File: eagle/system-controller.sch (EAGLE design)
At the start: 221 parts, among them IC1 TS4100, Q1 MOSFET-P-N-PAIR, Q10 MOSFET-P-N-PAIR, Q11 MOSFET-P-N-PAIR, Q12 MOSFET-P-N-PAIR, Q13 MOSFET-P-N-PAIR, Q14 MOSFET-P-N-PAIR, Q15 MOSFET-P-N-PAIR, Q16 MOSFET-P-N-PAIR, Q17 MOSFET-P-N-PAIR, Q18 MOSFET-P-N-PAIR, Q19 MOSFET-P-N-PAIR, Q2 MOSFET-P-N-PAIR, Q3 DNP/NTR4101P, Q4 DNP/NTR4101P, Q5 DNP/NTR4101P, Q6 DNP/NTR4101P, Q7 MOSFET-P-N-PAIR, Q8 MOSFET-P-N-PAIR, Q9 MOSFET-P-N-PAIR, SW1 TPS25944LRVCRWQFN-20-3X4, SW2 TPS25944LRVCRWQFN-20-3X4, SW3 TPS25944LRVCRWQFN-20-3X4, SW4 TPS25944LRVCRWQFN-20-3X4, SW5 TPS25944LRVCRWQFN-20-3X4, SW6 TPS25944LRVCRWQFN-20-3X4, SW7 TPS25944LRVCRWQFN-20-3X4, SW8 TPS25944LRVCRWQFN-20-3X4, U1 MEGA128-A, X1 8 MHz CRYSTAL-ABRACON-ABM3-SMD

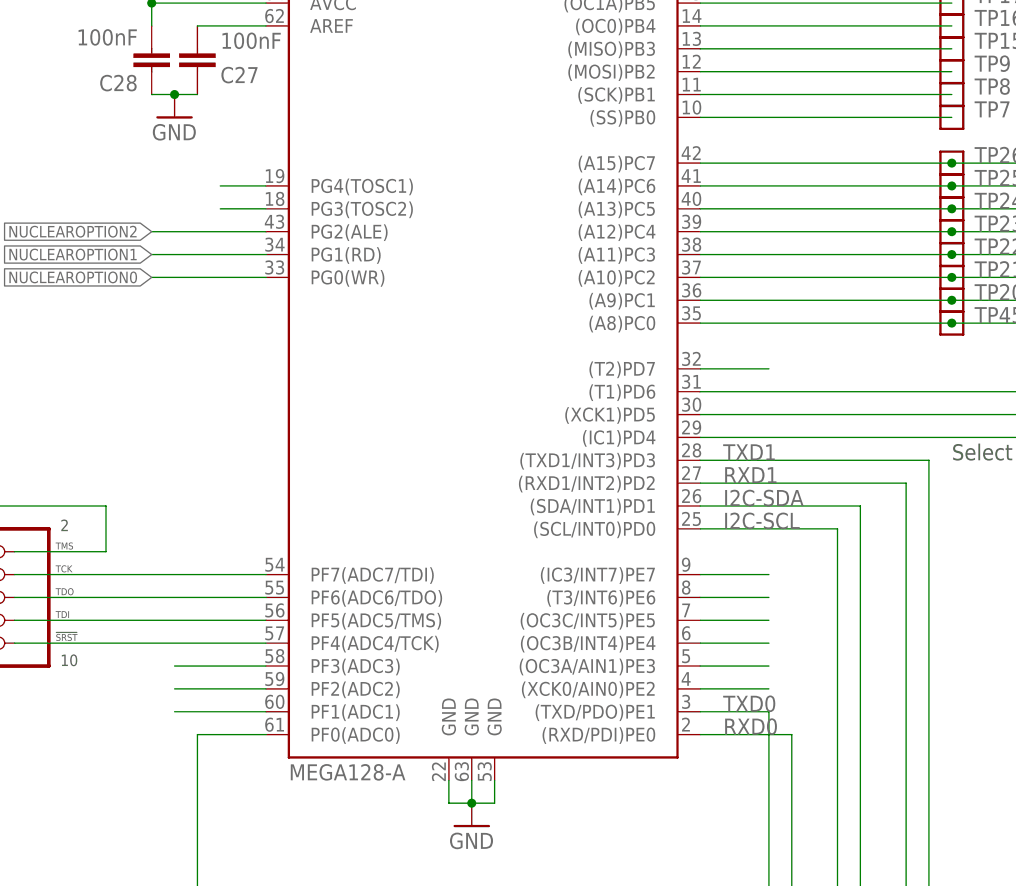
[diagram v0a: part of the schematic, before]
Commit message: added the remaining test points
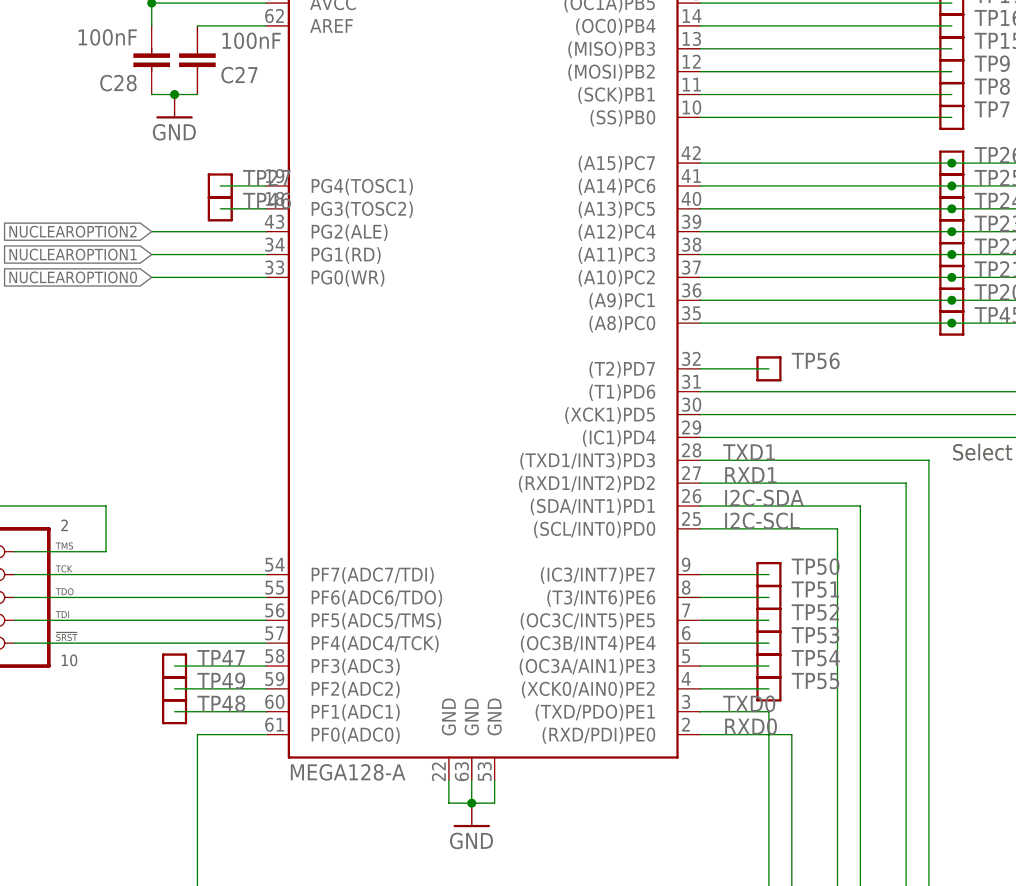
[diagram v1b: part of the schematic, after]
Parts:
- added TP27, TP46, TP47, TP48, TP49, TP50, TP51, TP52, TP53, TP54, TP55, TP56: TEST-POINT, Tova:TEST-POINT
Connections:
- net N$104: now also TP56.1
- net N$27: now also TP46.1
- net N$28: now also TP27.1
- net N$34: now also TP47.1
- net N$35: now also TP49.1
- net N$37: now also TP48.1
- net N$39: now also TP55.1
- net N$40: now also TP54.1
- net N$41: now also TP53.1
- net N$42: now also TP52.1
- net N$43: now also TP51.1
- net N$44: now also TP50.1
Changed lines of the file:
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@@
 <?xml version="1.0" encoding="utf-8"?>
 <!DOCTYPE eagle SYSTEM "eagle.dtd">
-<eagle version="7.3.0">
+<eagle version="7.5.0">
 <drawing>
 <settings>
@@
 <setting verticaltext="up"/>
 </settings>
-<grid distance="0.05" unitdist="inch" unit="inch" style="lines" multiple="2" display="yes" altdistance="0.01" altunitdist="inch" altunit="inch"/>
+<grid distance="0.1" unitdist="inch" unit="inch" style="lines" multiple="1" display="no" altdistance="0.01" altunitdist="inch" altunit="inch"/>
 <layers>
 <layer number="1" name="Top" color="4" fill="1" visible="no" active="no"/>
@@
 <attribute name="MPN" value="Vishay"/>
 </part>
+<part name="TP27" library="Tova" deviceset="TEST-POINT" device=""/>
+<part name="TP46" library="Tova" deviceset="TEST-POINT" device=""/>
+<part name="TP47" library="Tova" deviceset="TEST-POINT" device=""/>
+<part name="TP48" library="Tova" deviceset="TEST-POINT" device=""/>
+<part name="TP49" library="Tova" deviceset="TEST-POINT" device=""/>
+<part name="TP50" library="Tova" deviceset="TEST-POINT" device=""/>
+<part name="TP51" library="Tova" deviceset="TEST-POINT" device=""/>
+<part name="TP52" library="Tova" deviceset="TEST-POINT" device=""/>
+<part name="TP53" library="Tova" deviceset="TEST-POINT" device=""/>
+<part name="TP54" library="Tova" deviceset="TEST-POINT" device=""/>
+<part name="TP55" library="Tova" deviceset="TEST-POINT" device=""/>
+<part name="TP56" library="Tova" deviceset="TEST-POINT" device=""/>
 </parts>
 <sheets>
@@
 <attribute name="MPN" x="102.87" y="317.5" size="1.778" layer="96" rot="R180" display="off"/>
 </instance>
+<instance part="TP27" gate="G$1" x="149.86" y="220.98" smashed="yes">
+<attribute name="NAME" x="152.4" y="220.98" size="1.778" layer="95" font="vector"/>
+</instance>
+<instance part="TP46" gate="G$1" x="149.86" y="218.44" smashed="yes">
+<attribute name="NAME" x="152.4" y="218.44" size="1.778" layer="95" font="vector"/>
+</instance>
+<instance part="TP47" gate="G$1" x="144.78" y="167.64" smashed="yes">
+<attribute name="NAME" x="147.32" y="167.64" size="1.778" layer="95" font="vector"/>
+</instance>
+<instance part="TP48" gate="G$1" x="144.78" y="162.56" smashed="yes">
+<attribute name="NAME" x="147.32" y="162.56" size="1.778" layer="95" font="vector"/>
+</instance>
+<instance part="TP49" gate="G$1" x="144.78" y="165.1" smashed="yes">
+<attribute name="NAME" x="147.32" y="165.1" size="1.778" layer="95" font="vector"/>
+</instance>
+<instance part="TP50" gate="G$1" x="210.82" y="177.8" smashed="yes">
+<attribute name="NAME" x="213.36" y="177.8" size="1.778" layer="95" font="vector"/>
+</instance>
+<instance part="TP51" gate="G$1" x="210.82" y="175.26" smashed="yes">
+<attribute name="NAME" x="213.36" y="175.26" size="1.778" layer="95" font="vector"/>
+</instance>
+<instance part="TP52" gate="G$1" x="210.82" y="172.72" smashed="yes">
+<attribute name="NAME" x="213.36" y="172.72" size="1.778" layer="95" font="vector"/>
+</instance>
+<instance part="TP53" gate="G$1" x="210.82" y="170.18" smashed="yes">
+<attribute name="NAME" x="213.36" y="170.18" size="1.778" layer="95" font="vector"/>
+</instance>
+<instance part="TP54" gate="G$1" x="210.82" y="167.64" smashed="yes">
+<attribute name="NAME" x="213.36" y="167.64" size="1.778" layer="95" font="vector"/>
+</instance>
+<instance part="TP55" gate="G$1" x="210.82" y="165.1" smashed="yes">
+<attribute name="NAME" x="213.36" y="165.1" size="1.778" layer="95" font="vector"/>
+</instance>
+<instance part="TP56" gate="G$1" x="210.82" y="200.66" smashed="yes">
+<attribute name="NAME" x="213.36" y="200.66" size="1.778" layer="95" font="vector"/>
+</instance>
 </instances>
 <busses>
@@
 <pinref part="U1" gate="G$1" pin="PG3(TOSC2)"/>
 <wire x1="154.94" y1="218.44" x2="149.86" y2="218.44" width="0.1524" layer="91"/>
+<pinref part="TP46" gate="G$1" pin="1"/>
 </segment>
 </net>
@@
 <pinref part="U1" gate="G$1" pin="PG4(TOSC1)"/>
 <wire x1="154.94" y1="220.98" x2="149.86" y2="220.98" width="0.1524" layer="91"/>
+<pinref part="TP27" gate="G$1" pin="1"/>
 </segment>
 </net>
@@
 <pinref part="U1" gate="G$1" pin="PF3(ADC3)"/>
 <wire x1="154.94" y1="167.64" x2="144.78" y2="167.64" width="0.1524" layer="91"/>
+<pinref part="TP47" gate="G$1" pin="1"/>
 </segment>
 </net>
@@
 <pinref part="U1" gate="G$1" pin="PF2(ADC2)"/>
 <wire x1="144.78" y1="165.1" x2="154.94" y2="165.1" width="0.1524" layer="91"/>
+<pinref part="TP49" gate="G$1" pin="1"/>
 </segment>
 </net>
@@
 <pinref part="U1" gate="G$1" pin="PF1(ADC1)"/>
 <wire x1="154.94" y1="162.56" x2="144.78" y2="162.56" width="0.1524" layer="91"/>
+<pinref part="TP48" gate="G$1" pin="1"/>
 </segment>
 </net>
@@
 <pinref part="U1" gate="G$1" pin="(XCK0/AIN0)PE2"/>
 <wire x1="203.2" y1="165.1" x2="210.82" y2="165.1" width="0.1524" layer="91"/>
+<pinref part="TP55" gate="G$1" pin="1"/>
 </segment>
 </net>
@@
 <pinref part="U1" gate="G$1" pin="(OC3A/AIN1)PE3"/>
 <wire x1="203.2" y1="167.64" x2="210.82" y2="167.64" width="0.1524" layer="91"/>
+<pinref part="TP54" gate="G$1" pin="1"/>
 </segment>
 </net>
@@
 <pinref part="U1" gate="G$1" pin="(OC3B/INT4)PE4"/>
 <wire x1="203.2" y1="170.18" x2="210.82" y2="170.18" width="0.1524" layer="91"/>
+<pinref part="TP53" gate="G$1" pin="1"/>
 </segment>
 </net>
@@
 <pinref part="U1" gate="G$1" pin="(OC3C/INT5)PE5"/>
 <wire x1="203.2" y1="172.72" x2="210.82" y2="172.72" width="0.1524" layer="91"/>
+<pinref part="TP52" gate="G$1" pin="1"/>
 </segment>
 </net>
@@
 <pinref part="U1" gate="G$1" pin="(T3/INT6)PE6"/>
 <wire x1="203.2" y1="175.26" x2="210.82" y2="175.26" width="0.1524" layer="91"/>
+<pinref part="TP51" gate="G$1" pin="1"/>
 </segment>
 </net>
@@
 <pinref part="U1" gate="G$1" pin="(IC3/INT7)PE7"/>
 <wire x1="203.2" y1="177.8" x2="210.82" y2="177.8" width="0.1524" layer="91"/>
+<pinref part="TP50" gate="G$1" pin="1"/>
 </segment>
 </net>
@@
 <pinref part="U1" gate="G$1" pin="(T2)PD7"/>
 <wire x1="203.2" y1="200.66" x2="210.82" y2="200.66" width="0.1524" layer="91"/>
+<pinref part="TP56" gate="G$1" pin="1"/>
 </segment>
 </net>

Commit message: working on board layout. Have everything organized in in general location. Working on routing.
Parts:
- removed C10, C18, C20, C22, C24: TBD, rcl_custom:C-EU0603-B-NOSILK
- removed C19, C29: 1uF, rcl_custom:C-EU0603-B-NOSILK
- removed LED13, LED14, LED15: DNP/AMB, psas_c3_team05:LED-0603
- removed Q14, Q15, Q16, Q17, Q18, Q19, Q8: MOSFET-P-N-PAIR, ic-transistor-mosfet-n-p:MOSFET-P-N-PAIR
- removed Q20: (no value), adafruit:MOSFET-NREFLOW
- removed R47, R53: 4.7k, rcl_custom:R-US_0603-B-NOSILK
- removed R48, R49, R54, R55: 47k, rcl_custom:R-US_0603-B-NOSILK
- removed R51, R56: 1k, rcl_custom:R-US_0603-B-NOSILK
- removed RUVLO1, RUVLO2, RUVLO3, RUVLO4, RUVLO5, RUVLO6, RUVLO7, RUVLO8: 93.1k, rcl_custom:R-US_0603-B-NOSILK
- removed SW8: TPS25944LRVCRWQFN-20-3X4, WQFN-20-3x4:TPS25944LRVCRWQFN-20-3X4
- removed TP1: TPSPAD1-13, testpad:TPSPAD1-13
- added CFUSE3A: 1uF, rcl_custom:C-EU0603-B-NOSILK
- added CFUSE7: TBD, rcl_custom:C-EU0603-B-NOSILK
- added CLDO3: 2.2uF, rcl_custom:C-EU0603-B-NOSILK
- added CPHOTO0A, CPHOTO1B, CPHOTO3A, CPHOTO3B: 100nF, rcl_custom:C-EU0603-B-NOSILK
- added LED0, LED4, LED5: GRN, psas_c3_team05:LED-0603
- added Q0: MOSFET-P-N-PAIR, ic-transistor-mosfet-n-p:MOSFET-P-N-PAIR
- added R0/UVLO, R1/UVLO, R2/UVLO, R3/UVLO, R4/UVLO, R5/UVLO, R6/UVLO, R7/UVLO: 47k, rcl_custom:R-US_0603-B-NOSILK
- added RLDO1: 10k, rcl_custom:R-US_0603-B-NOSILK
- added RPHOTO0A, RPHOTO0B, RPHOTO1A, RPHOTO2A, RPHOTO2B, RPHOTO3A, RPHOTO3B: 390, rcl_custom:R-US_0603-B-NOSILK
- added SW0: TPS25944LRVCRWQFN-20-3X4, WQFN-20-3x4:TPS25944LRVCRWQFN-20-3X4
- added TPLDOA: TEST-POINT, Tova:TEST-POINT
- C11, C13, C15, C17, C9: value 1uF -> TBD; DIST digikey -> (none); DPN 1276-1946-1-ND -> (none); MFN Samsung -> (none); MPN CL10B105KP8NNNC -> (none)
- C12, C14, C16: value TBD -> 1uF; DIST (none) -> digikey; DPN (none) -> 1276-1946-1-ND; MFN (none) -> Samsung; MPN (none) -> CL10B105KP8NNNC
- C2: value 100nF -> 1uF; DPN 399-1097-1-ND -> 1276-1946-1-ND; MFN Kemet -> Samsung; MPN C0603C104J4RACTU -> CL10B105KP8NNNC
- C3: value 100nF -> TBD; DIST digikey -> (none); DPN 490-6327-1-ND -> (none); MFN Murata -> (none); MPN GRM155R71C104JA88D -> (none)
- C4: value 2.2uF -> 1uF; DPN 1276-1183-1-ND -> 1276-1946-1-ND; MPN CL10A225KQ8NNNC -> CL10B105KP8NNNC
- C5: value 100nF -> TBD; DIST digikey -> (none); DPN 399-1097-1-ND -> (none); MFN Kemet -> (none); MPN C0603C104J4RACTU -> (none)
- C6: value 100nF -> 1uF; DPN 490-6327-1-ND -> 1276-1946-1-ND; MFN Murata -> Samsung; MPN GRM155R71C104JA88D -> CL10B105KP8NNNC
- LED10, LED11, LED12, LED9: value GRN -> DNP/AMB; DPN 732-4971-1-ND -> 475-2712-1-ND; MFN Wurth Electronics INC. -> OSRAM Opto Semi,; MPN 150060GS75000 -> LA L296-Q2R2-1-Z
- LED6: value DNP/AMB -> GRN; DPN 475-2712-1-ND -> 732-4971-1-ND; MFN OSRAM Opto Semi, -> Wurth Electronics INC.; MPN LA L296-Q2R2-1-Z -> 150060GS75000
- Q10, Q11, Q12, Q9: value MOSFET-P-N-PAIR -> DNP/NTR4101P; device ic-transistor-mosfet-n-p:MOSFET-P-N-PAIR -> Tova:NTR4101P; DPN DMG6601LVT-7DICT-ND -> NTR4101PT1HOSCT-ND; MFN Diodes Incorporated -> ON Semiconductor; MPN DMG6601LVT-7 -> NTR4101PT1H
- Q13: value MOSFET-P-N-PAIR -> (none); device ic-transistor-mosfet-n-p:MOSFET-P-N-PAIR -> adafruit:MOSFET-NREFLOW; DIST digikey -> (none); DPN DMG6601LVT-7DICT-ND -> (none); MFN Diodes Incorporated -> (none); MPN DMG6601LVT-7 -> (none)
- Q3, Q4, Q5, Q6: value DNP/NTR4101P -> MOSFET-P-N-PAIR; device Tova:NTR4101P -> ic-transistor-mosfet-n-p:MOSFET-P-N-PAIR; DPN NTR4101PT1HOSCT-ND -> DMG6601LVT-7DICT-ND; MFN ON Semiconductor -> Diodes Incorporated; MPN NTR4101PT1H -> DMG6601LVT-7
- R1, R3, R7: value 390 -> 47k; DPN A103093CT-ND -> 1276-4808-1-ND; MFN TE -> Samaung; MPN 4-1676481-5 -> RC1608F473CS
- R10, R5: value 390 -> 93.1k; DPN A103093CT-ND -> 1276-4837-1-ND; MFN TE -> Samsung; MPN 4-1676481-5 -> RC1608F9312CS
- R12: value 10k -> 1k; DPN 1276-3485-1-ND -> 1276-3484-1-ND; MPN RC1608F103CS -> RC1608F102CS
- R14, R20, R28, R33, R38, R43: value 47k -> 4.7k; DPN 1276-4808-1-ND -> 1276-3502-1-ND; MFN Samaung -> Samsung; MPN RC1608F473CS -> RC1608F472CS
- R15, R21: value 1k -> 47k; DPN 1276-3484-1-ND -> 1276-4808-1-ND; MFN Samsung -> Samaung; MPN RC1608F102CS -> RC1608F473CS
- R16, R25: value 47k -> 93.1k; DPN 1276-4808-1-ND -> 1276-4837-1-ND; MFN Samaung -> Samsung; MPN RC1608F473CS -> RC1608F9312CS
- R18: value 4.7k -> 1k; DPN 1276-3502-1-ND -> 1276-3484-1-ND; MPN RC1608F472CS -> RC1608F102CS
- R2, R8: value 390 -> 4.7k; DPN A103093CT-ND -> 1276-3502-1-ND; MFN TE -> Samsung; MPN 4-1676481-5 -> RC1608F472CS
- R26, R31, R36, R41, R46, R6: value 47k -> 1k; DPN 1276-4808-1-ND -> 1276-3484-1-ND; MFN Samaung -> Samsung; MPN RC1608F473CS -> RC1608F102CS
- R27, R32, R37, R42, R9: value 4.7k -> 47k; DPN 1276-3502-1-ND -> 1276-4808-1-ND; MFN Samsung -> Samaung; MPN RC1608F472CS -> RC1608F473CS
- R30, R35, R40, R45: value 1k -> 93.1k; DPN 1276-3484-1-ND -> 1276-4837-1-ND; MPN RC1608F102CS -> RC1608F9312CS
- SW1: DIST digikey -> (none); DPN 296-42152-1-ND -> (none); MFN TPS25944LRVCR -> (none); MPN Texas Instruments -> (none)
- renumbered C21 to CFUSE7A, C23 to CLDO1, C31 to CHWWD, C40 to CLDO2, LED8 to LED3, R11 to RA4, R17 to RA2, R50 to RA1, R52 to RHWWD0, R57 to RA3, R58 to RA5, R59 to RA7, R60 to RA8, R62 to RA6, R63 to RPHOTO1B, R64 to RHWWD1, R65 to RHWWD2, R66 to RHWWD4, R67 to RHWWD3, RILIM to RILIM0, RIMON to RIMON0, TP28 to TP0GHT, TP29 to TP1GOOD, TP30 to TP1GHT, TP31 to TP2GOOD, TP32 to TP2GHT, TP33 to TP3GOOD, TP34 to TP3GHT, TP35 to TP4GOOD, TP36 to TP4GHT, TP37 to TP5GOOD, TP38 to TP5GHT, TP39 to TP6GOOD, TP40 to TP6GHT, TP41 to TP7GOOD, TP42 to TP7GHT, TP5 to TP0GOOD
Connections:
- removed net N$31: C10.1, SW1.DV/DT
- removed net N$7: Q2A.D, Q2B.G, R14.2
- new net C10\: CFUSE3A.2, Q3B.S, R19.1, SW3.IN
- new net INOF: C3.1, SW0.DV/DT
- new net N$110: Q7B.D, R45.1
- new net N$111: Q6B.D, R40.1
- net 3V: now also CLDO3.1, CPHOTO1B.2, CPHOTO3B.2, Q10.S, Q11.S, Q12.S, Q9.S, U$2.VDD; no longer C2.2, C4.1, C6.2, Q3.S, Q4.S, Q5.S, Q6.S, U$3.VDD
- net GND: now also C11.2, C12.1, C13.2, C14.1, C15.2, C16.1, C17.2, C3.2, C4.1, C5.2, C9.2, CFUSE3A.1, CFUSE7.2, CLDO3.2, CPHOTO0A.1, CPHOTO1B.1, CPHOTO3A.1, CPHOTO3B.1, LED0.K, LED4.K, LED5.K, Q0A.S, Q13.S, Q3A.S, Q4A.S, Q5A.S, Q6A.S, R0/UVLO.2, R1/UVLO.2, R15.2, R2/UVLO.2, R21.2, R29.2, R3.2, R3/UVLO.2, R34.2, R39.2, R4/UVLO.2, R44.2, R5/UVLO.2, R6/UVLO.2, R7/UVLO.2, R9.2, SW0.DMODE, SW0.GND, SW0.OVP, SW0.PGHT; no longer C10.2, C11.1, C12.2, C13.1, C14.2, C15.1, C16.2, C17.1, C18.2, C19.1, C20.2, C22.2, C24.2, C29.1, C3.1, C4.2, C5.1, C9.1, LED13.K, LED14.K, LED15.K, Q10A.S, Q11A.S, Q12A.S, Q20.S, Q8A.S, Q9A.S, R13.2, R16.2, R19.2, R25.2, R26.2, R28.2, R31.2, R33.2, R36.2, R38.2, R41.2, R43.2, R46.2, R48.2, R54.2, R6.2, SW8.DMODE, SW8.GND, SW8.OVP, SW8.PGHT
- net N$10: now also R16.2, R2/UVLO.1, SW2.EN/UVLO; no longer R41.1, RUVLO2.2, SW3.EN/UVLO
- net N$100: now also RILIM6.1, SW6.ILIM; no longer RILIM7.1, SW8.ILIM
- net N$101: now also SW6.PGOOD; no longer SW8.PGOOD
- net N$102: now also C17.1, SW6.DV/DT; no longer C24.1, SW8.DV/DT
- net N$103: now also Q6A.G, R38.2, R39.1; no longer Q11A.G, R19.1, R47.2
- net N$105: now also Q6A.D, Q6B.G, R37.2; no longer Q11A.D, Q18B.G, R49.2
- net N$106: now also Q13.G; no longer Q20.G
- net N$108: now also Q5B.D, R35.1; no longer Q19B.D, RUVLO8.1
- net N$16: now also RPHOTO2A.2, U$3.VOUT; no longer R1.2, U$2.VOUT
- net N$18: now also RPHOTO3B.1; no longer R8.1
- net N$19: now also SW2.ILIM; no longer SW3.ILIM
- net N$2: now also Q1B.D, R10.1; no longer Q2A.G, R54.1, R9.2
- net N$20: now also RPHOTO3A.2; no longer R7.2
- net N$21: now also SW0.ILIM; no longer SW1.ILIM
- net N$22: now also RLDO1.2, TPLDOA.1; no longer R12.2, TP1.PP
- net N$24: now also U$2.VOUT; no longer U$3.VOUT
- net N$25: now also SW0.PGOOD; no longer SW1.PGOOD
- net N$26: now also LED0.A, R6.2; no longer LED1.A, R15.2
- net N$29: now also R1/UVLO.1, R10.2, SW1.EN/UVLO; no longer R46.1, RUVLO1.2, SW2.EN/UVLO
- net N$3: now also R0/UVLO.1, R5.2; no longer Q13B.D, RUVLO1.1
- net N$30: now also SW1.ILIM; no longer SW2.ILIM
- net N$32: now also SW1.PGOOD; no longer SW2.PGOOD
- net N$38: now also C5.1, SW1.DV/DT; no longer C12.1, SW2.DV/DT
- net N$4: now also RPHOTO2B.1, U$3.VIN; no longer R10.1, U$2.VIN
- net N$45: now also LED1.A, R12.2; no longer LED2.A, R21.2
- net N$49: now also R8.2, R9.1; no longer R18.2, R48.1
- net N$5: now also RPHOTO0A.2; no longer R2.2
- net N$50: now also Q0A.G, R3.1; no longer Q14B.D, RUVLO2.1
- net N$51: now also Q1B.G, R7.2; no longer Q13B.G, R20.2
- net N$52: now also LED2.A, R18.2; no longer LED7.A, R30.2
- net N$53: now also LED12.A; no longer LED15.A
- net N$54: now also Q11.D; no longer Q4.D
- net N$55: now also Q12.D; no longer Q3.D
- net N$56: now also LED11.A; no longer LED14.A
- net N$57: now also LED9.A; no longer LED6.A
- net N$58: now also Q9.D; no longer Q6.D
- net N$59: now also SW2.PGOOD; no longer SW3.PGOOD
- net N$6: now also RPHOTO0B.1; no longer R3.1
- net N$60: now also LED10.A; no longer LED13.A
- net N$61: now also Q10.D; no longer Q5.D
- net N$62: now also C9.1, SW2.DV/DT; no longer C14.1, SW3.DV/DT
- net N$63: now also Q2A.G, R14.2, R15.1; no longer Q7A.G, R27.2, R43.1
- net N$64: now also R16.1; no longer RUVLO3.1
- net N$65: now also Q2A.D, Q2B.G, R13.2; no longer Q14B.G, Q7A.D, R29.2
- net N$66: now also R26.2; no longer R35.2
- net N$67: now also R45.2, R7/UVLO.1, SW7.EN/UVLO; no longer R16.1, RUVLO8.2, SW4.EN/UVLO
- net N$68: now also RILIM7.1, SW7.ILIM; no longer RILIM3.1, SW4.ILIM
- net N$69: now also SW7.PGOOD; no longer SW4.PGOOD
- net N$70: now also CFUSE7.1, SW7.DV/DT; no longer C16.1, SW4.DV/DT
- net N$71: now also Q7A.G, R43.2, R44.1; no longer Q12A.G, R13.1, R53.2
- net N$72: now also Q0A.D, Q0B.G, R1.2; no longer Q15B.D, RUVLO4.1
- net N$73: now also Q7A.D, Q7B.G, R42.2; no longer Q12A.D, Q19B.G, R55.2
- net N$74: now also LED4.A, R31.2; no longer LED9.A, R40.2
- net N$75: now also R35.2, R5/UVLO.1; no longer R26.1, RUVLO6.2
- net N$76: now also RILIM5.1; no longer RILIM4.1
- net N$78: now also C15.1; no longer C18.1
- net N$79: now also Q5A.G, R33.2, R34.1; no longer Q10A.G, R28.1, R42.2
- net N$8: now also RPHOTO1A.2, U$2.VIN; no longer R5.2, U$3.VIN
- net N$80: now also Q0B.D, R5.1; no longer Q16B.D, RUVLO5.1
- net N$81: now also Q5A.D, Q5B.G, R32.2; no longer Q10A.D, Q17B.G, R44.2
- net N$82: now also LED5.A, R36.2; no longer LED10.A, R45.2
- net N$83: now also R30.2, R4/UVLO.1, SW4.EN/UVLO; no longer R31.1, RUVLO5.2, SW6.EN/UVLO
- net N$84: now also RILIM4.1, SW4.ILIM; no longer RILIM5.1, SW6.ILIM
- net N$85: now also SW4.PGOOD; no longer SW6.PGOOD
- net N$86: now also C13.1, SW4.DV/DT; no longer C20.1, SW6.DV/DT
- net N$87: now also Q4A.G, R28.2, R29.1; no longer Q9A.G, R33.1, R37.2
- net N$88: now also Q3B.D, R25.1; no longer Q17B.D, RUVLO6.1
- net N$89: now also Q4A.D, Q4B.G, R27.2; no longer Q16B.G, Q9A.D, R39.2
- net N$9: now also SW0.EN/UVLO; no longer R6.1, RUVLO3.2, SW1.EN/UVLO
- net N$90: now also LED6.A, R41.2; no longer LED11.A, R51.2
- net N$91: now also R25.2, R3/UVLO.1, SW3.EN/UVLO; no longer R36.1, RUVLO4.2, SW7.EN/UVLO
- net N$92: now also RILIM3.1, SW3.ILIM; no longer RILIM6.1, SW7.ILIM
- net N$93: now also SW3.PGOOD; no longer SW7.PGOOD
- net N$94: now also C11.1, SW3.DV/DT; no longer C22.1, SW7.DV/DT
- net N$95: now also Q3A.G, R20.2, R21.1; no longer Q8A.G, R32.2, R38.1
- net N$96: now also Q4B.D, R30.1; no longer Q18B.D, RUVLO7.1
- net N$97: now also Q3A.D, Q3B.G, R19.2; no longer Q15B.G, Q8A.D, R34.2
- net N$98: now also LED7.A, R46.2; no longer LED12.A, R56.2
- net N$99: now also R40.2, R6/UVLO.1, SW6.EN/UVLO; no longer R25.1, RUVLO7.2, SW8.EN/UVLO
- net NUCLEAROPTION_OUT: now also Q13.D; no longer Q20.D
- net PCB3_EN: now also R20.1; no longer R32.1
- net RXD0: now also Q12.G, RPHOTO3B.2; no longer Q3.G, R8.2
- net RXD1: now also Q10.G; no longer Q5.G
- net TXD0: now also Q11.G, RPHOTO2B.2; no longer Q4.G, R10.2
- net TXD1: now also Q9.G, RPHOTO0B.2; no longer Q6.G, R3.2
- net UART_FC_RX: now also RPHOTO0A.1; no longer R2.1
- net UART_FC_TX: now also RPHOTO1A.1; no longer R5.1
- net UART_FC_VCC: now also CPHOTO0A.2; no longer C5.2
- net UART_LGR_RX: now also RPHOTO2A.1; no longer R1.1
- net UART_LGR_TX: now also RPHOTO3A.1; no longer R7.1
- net UART_LGR_VCC: now also CPHOTO3A.2, U$3.VDD; no longer C3.2, U$2.VDD
- net V+: now also RLDO1.1; no longer R12.1
- net VBC1: now also R12.1, SW1.OUT; no longer R21.1, SW2.OUT
- net VBC2: now also R18.1, SW2.OUT; no longer R30.1, SW3.OUT
- net VBC4: now also R31.1, SW4.OUT; no longer R40.1, SW6.OUT
- net VBC5: now also R36.1; no longer R45.1
- net VBC6: now also R41.1, SW6.OUT; no longer R51.1, SW8.OUT
- net VBC7: now also R46.1, SW7.OUT; no longer R56.1, SW4.OUT
- net VBUS: now also C12.2, C14.2, C16.2, C2.2, C4.2, C6.2, Q0B.S, Q1B.S, Q4B.S, Q5B.S, Q6B.S, Q7B.S, R1.1, R13.1, R27.1, R32.1, R37.1, R42.1, R7.1; no longer C11.2, C13.2, C15.2, C17.2, C19.2, C29.2, C9.2, Q13B.S, Q14B.S, Q15B.S, Q16B.S, Q17B.S, Q18B.S, Q19B.S, R14.1, R20.1, R29.1, R34.1, R39.1, R44.1, R49.1, R55.1, SW3.IN, SW8.IN
- net VCB0: now also R6.1, SW0.OUT; no longer R15.1, SW1.OUT
- net VCB0_!FLT: now also SW0.!FLT; no longer SW1.!FLT
- net VCB0_EN: now also R2.1; no longer R9.1
- net VCB0_IMON: now also SW0.IMON; no longer SW1.IMON
- net VCB1_!FLT: now also SW1.!FLT; no longer SW2.!FLT
- net VCB1_EN: now also R8.1; no longer R18.1
- net VCB1_IMON: now also SW1.IMON; no longer SW2.IMON
- net VCB2_!FLT: now also SW2.!FLT; no longer SW3.!FLT
- net VCB2_EN: now also R14.1; no longer R27.1
- net VCB2_IMON: now also SW2.IMON; no longer SW3.IMON
- net VCB3: now also R26.1, SW3.OUT; no longer R35.1, SW7.OUT
- net VCB3_!FLT: now also SW3.!FLT; no longer SW7.!FLT
- net VCB3_IMON: now also RIMON3.1, SW3.IMON; no longer RIMON6.1, SW7.IMON
- net VCB4_!FLT: now also SW4.!FLT; no longer SW6.!FLT
- net VCB4_EN: now also R28.1; no longer R37.1
- net VCB4_IMON: now also RIMON4.1, SW4.IMON; no longer RIMON5.1, SW6.IMON
- net VCB5_EN: now also R33.1; no longer R42.1
- net VCB5_IMON: now also RIMON5.1; no longer RIMON4.1
- net VCB6_!FLT: now also SW6.!FLT; no longer SW8.!FLT
- net VCB6_EN: now also R38.1; no longer R47.1
- net VCB6_IMON: now also RIMON6.1, SW6.IMON; no longer RIMON7.1, SW8.IMON
- net VCB7_!FLT: now also SW7.!FLT; no longer SW4.!FLT
- net VCB7_EN: now also R43.1; no longer R53.1
- net VCB7_IMON: now also RIMON7.1, SW7.IMON; no longer RIMON3.1, SW4.IMON
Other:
- moved on the sheet: C11, C12, C13, C14, C15, C16, C17, C2, C3, C4, C5, C6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

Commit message: Pushing newest changes to the board layout
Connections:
- removed net C10\: CFUSE3A.2, Q3B.S, R19.1, SW3.IN
- removed net N$3: R0/UVLO.1, R5.2
- new net GMD: LED0.K
- net GND: no longer LED0.K
- net N$9: now also R0/UVLO.1, R5.2
- net VBUS: now also CFUSE3A.2, Q3B.S, R19.1, SW0.IN, SW3.IN

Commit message: latetest changes pushed
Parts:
- removed LED12: DNP/AMB, psas_c3_team05:LED-0603
- removed RA8: 47k, rcl_custom:R-US_0603-B-NOSILK
- added LED8: DNP/AMB, psas_c3_team05:LED-0603
- added RA0: 47k, rcl_custom:R-US_0603-B-NOSILK
- added TP28, TP29, TP30, TP31, TP32, TP33, TP34, TP5: TEST-POINT, Tova:TEST-POINT
- CN1: value TBD -> 22u
- J1: value (none) -> 1
- Q13: value (none) -> DON3035L
- RILIM0, RILIM1, RILIM2, RILIM3, RILIM4, RILIM5, RILIM6, RILIM7: value TBD -> 47k; DIST (none) -> digikey; DPN (none) -> 1276-4808-1-ND; MFN (none) -> Samaung; MPN (none) -> RC1608F473CS
- RN1, RN2, RN3: value TBD -> 390; DPN 1276-3502-1-ND -> A103093CT-ND; MFN Samsung -> TE; MPN RC1608F472CS -> 4-1676481-5
- RN4: value 1k -> 10k
- RNR: value TBD -> 470k
- renumbered CFUSE7 to C19, CFUSE7A to C20, CHWWD to CN1, RHWWD0 to RN1, RHWWD1 to RN2, RHWWD2 to RN3, RHWWD3 to RN4, RHWWD4 to RNR
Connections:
- net VBC1 renamed VCB1
- net VBC2 renamed VCB2
- net VBC4 renamed VCB4
- net VBC5 renamed VCB5
- net VBC6 renamed VCB6
- net VBC7 renamed VCB7
- removed net GMD: LED0.K
- net 3V: now also RA0.1; no longer RA8.1
- net GND: now also LED0.K, LED8.K; no longer LED12.K
- net I2C-SCL: now also TP5.1
- net I2C-SDA: now also TP28.1
- net N$50: now also R2.2
- net N$53: now also LED11.A; no longer LED12.A
- net N$56: now also LED10.A; no longer LED11.A
- net N$57: now also LED8.A; no longer LED9.A
- net N$60: now also LED9.A; no longer LED10.A
- net UART_FC_RX: now also TP30.1
- net UART_FC_TX: now also TP31.1
- net UART_FC_VCC: now also TP29.1
- net UART_LGR_RX: now also TP33.1
- net UART_LGR_TX: now also TP34.1
- net UART_LGR_VCC: now also TP32.1
- net VCB0_!FLT: now also RA0.2; no longer RA1.2
- net VCB1_!FLT: now also RA1.2; no longer RA2.2
- net VCB2_!FLT: now also RA2.2; no longer RA3.2
- net VCB3_!FLT: now also RA3.2; no longer RA4.2
- net VCB4_!FLT: now also RA4.2; no longer RA5.2
- net VCB5_!FLT: now also RA5.2; no longer RA6.2
- net VCB6_!FLT: now also RA6.2; no longer RA7.2
- net VCB7_!FLT: now also RA7.2; no longer RA8.2
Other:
- note added: "ILIM = 89/RILIM (kOhms)"
- note added: "N-Channel MOSFET DON3053L V_TH min = 0.6V V_TH max = 1.4V"
- note added: "Todo: Determine ILIM for each switch Set RILIM resistors to 47k which gives about 1.9A limit"
- note removed: "ILIM = 89/RILIM"
- note removed: "Todo: Determine ILIM for each switch"
- moved on the sheet: J1, LED10, LED11, LED9, RA1, RA2, RA3, RA4, RA5, RA6, RA7

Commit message: latest changes... thicker polys, moved some traces, more...
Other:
- note added: "P-Channel MOSFET"
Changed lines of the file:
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@@
 V_TH min = 0.6V
 V_TH max = 1.4V</text>
+<text x="233.68" y="132.08" size="1.778" layer="97">P-Channel MOSFET</text>
 </plain>
 <instances>
